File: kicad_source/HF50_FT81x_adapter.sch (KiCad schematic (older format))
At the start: 2 parts

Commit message: made layout
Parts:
- P1: renamed from P?; footprint mechanical-connectors:DSUB-9_Female_Horizontal_P2.77x2.84mm_EdgePinOffset7.70mm_Housed_MountingHolesOffset9.12mm -> Connector_Dsub:DSUB-9_Male_Horizontal_P2.77x2.84mm_EdgePinOffset7.70mm_Housed_MountingHolesOffset9.12mm
- P2: renamed from P?; footprint (none) -> mechanical-connectors:MiniDIN_8
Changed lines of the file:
@@
 $EndDescr
 $Comp
-L mechanical-connectors:CONN_01X09 P?
+L mechanical-connectors:CONN_01X09 P1
 U 1 1 609D1868
 P 3400 3250
-F 0 "P?" H 3317 3865 50  0000 C CNN
+F 0 "P1" H 3317 3865 50  0000 C CNN
 F 1 "CONN_01X09" H 3317 3774 50  0000 C CNN
-F 2 "mechanical-connectors:DSUB-9_Female_Horizontal_P2.77x2.84mm_EdgePinOffset7.70mm_Housed_MountingHolesOffset9.12mm" H 3400 3250 50  0001 C CNN
+F 2 "Connector_Dsub:DSUB-9_Male_Horizontal_P2.77x2.84mm_EdgePinOffset7.70mm_Housed_MountingHolesOffset9.12mm" H 3400 3250 50  0001 C CNN
 F 3 "" H 3400 3250 50  0000 C CNN
 	1    3400 3250
@@
 $EndComp
 $Comp
-L mechanical-connectors:CONN_01X08 P?
+L mechanical-connectors:CONN_01X08 P2
 U 1 1 609D1DBC
 P 7450 3400
-F 0 "P?" H 7528 3441 50  0000 L CNN
+F 0 "P2" H 7528 3441 50  0000 L CNN
 F 1 "CONN_01X08" H 7528 3350 50  0000 L CNN
-F 2 "" H 7450 3400 50  0000 C CNN
+F 2 "mechanical-connectors:MiniDIN_8" H 7450 3400 50  0001 C CNN
 F 3 "" H 7450 3400 50  0000 C CNN
 	1    7450 3400
@@
 PTT
 $Comp
-L power-supply:GND #PWR?
+L power-supply:GND #PWR01
 U 1 1 609D3626
 P 3800 3750
-F 0 "#PWR?" H 3800 3500 50  0001 C CNN
+F 0 "#PWR01" H 3800 3500 50  0001 C CNN
 F 1 "GND" H 3805 3577 50  0000 C CNN
 F 2 "" H 3800 3750 50  0000 C CNN
@@
 NoConn ~ 3600 3650
 $Comp
-L power-supply:GND #PWR?
+L power-supply:GND #PWR02
 U 1 1 609D3D93
 P 7100 3850
-F 0 "#PWR?" H 7100 3600 50  0001 C CNN
+F 0 "#PWR02" H 7100 3600 50  0001 C CNN
 F 1 "GND" H 7105 3677 50  0000 C CNN
 F 2 "" H 7100 3850 50  0000 C CNN

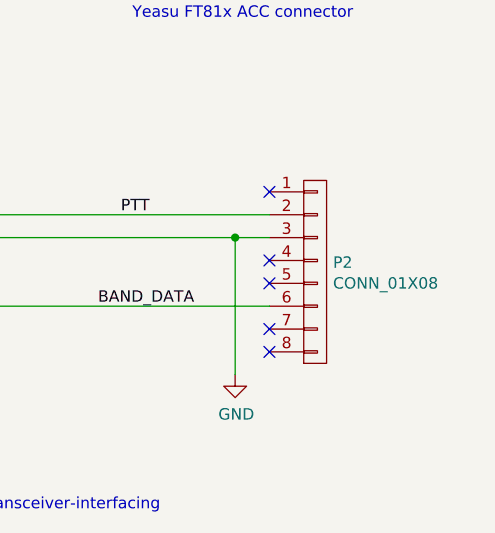
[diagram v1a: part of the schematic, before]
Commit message: added pdf schematic
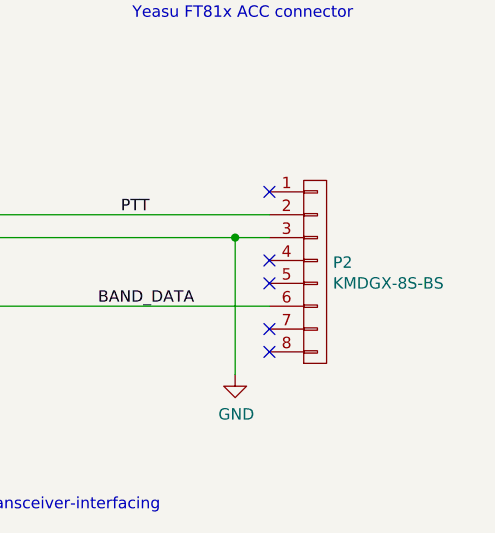
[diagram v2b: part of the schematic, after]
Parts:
- P2: value CONN_01X08 -> KMDGX-8S-BS
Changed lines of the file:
@@
 P 7450 3400
 F 0 "P2" H 7528 3441 50  0000 L CNN
-F 1 "CONN_01X08" H 7528 3350 50  0000 L CNN
+F 1 "KMDGX-8S-BS" H 7528 3350 50  0000 L CNN
 F 2 "mechanical-connectors:MiniDIN_8" H 7450 3400 50  0001 C CNN
 F 3 "" H 7450 3400 50  0000 C CNN

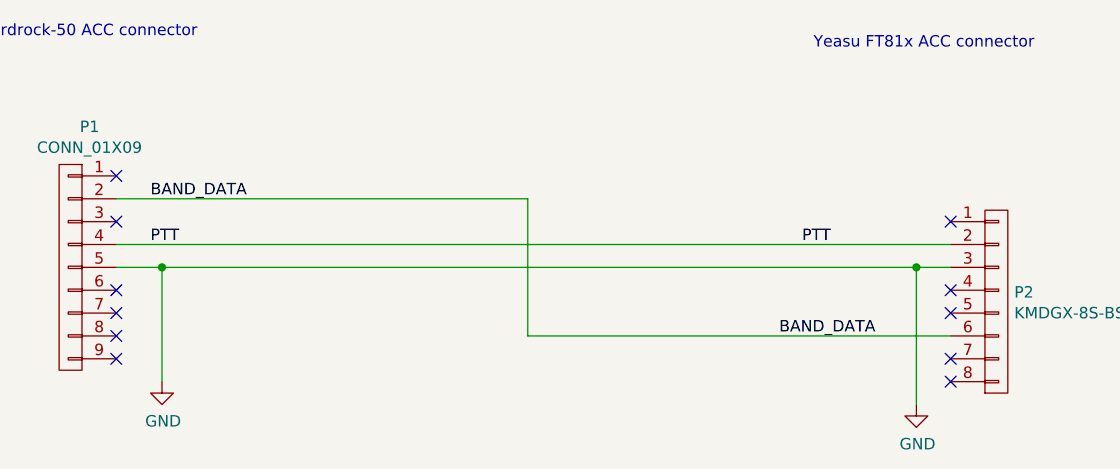
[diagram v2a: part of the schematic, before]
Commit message: added LED
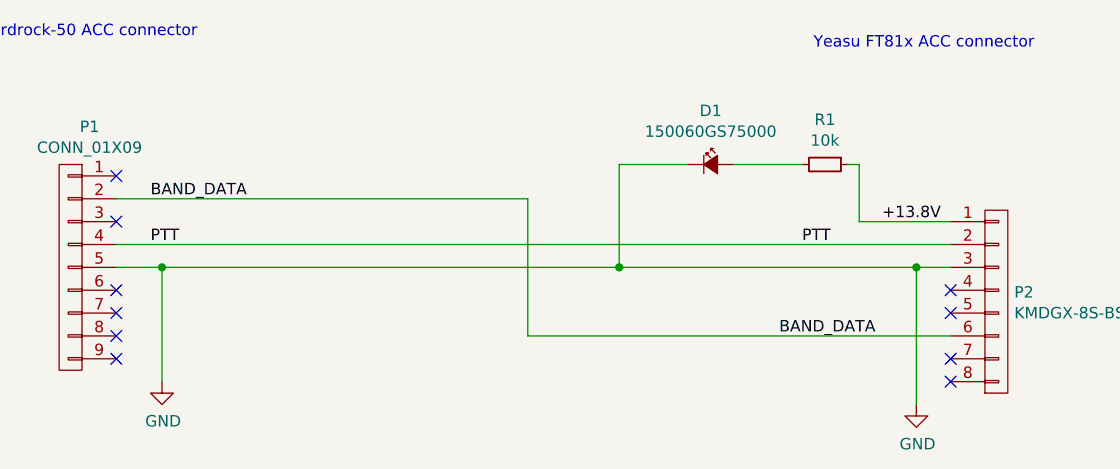
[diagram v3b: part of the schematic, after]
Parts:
- added D1: 150060GS75000, LEDs:LED_0603, symbol devices:Led_Small
- added R1: 10k, resistors:R_0603, symbol devices:R_0603
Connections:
- net GND: now also D1.1 (K)
- net +13.8V: now reaches P2.1 (P1)
- net +13.8V: now also R1.1
- new net: D1.2 (A), R1.2
- no-connect marks 11 -> 10
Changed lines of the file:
@@
 Sheet 1 1
 Title "Hardrock HF50 to Yaesu FT81x adapter"
-Date "2021-05-13"
+Date "2021-05-20"
 Rev "0.1"
 Comp "generationmake"
@@
 	3600 3150 7250 3150
 Wire Wire Line
-	7100 3250 3800 3250
+	7100 3250 5800 3250
 Connection ~ 7100 3250
 Connection ~ 3800 3250
@@
 Wire Wire Line
 	3600 2950 5400 2950
-NoConn ~ 7250 3050
 NoConn ~ 7250 3350
 NoConn ~ 7250 3450
@@
 Wire Wire Line
 	5400 3550 7250 3550
+$Comp
+L devices:R_0603 R1
+U 1 1 60A60105
+P 6700 2800
+F 0 "R1" V 6504 2800 50  0000 C CNN
+F 1 "10k" V 6595 2800 50  0000 C CNN
+F 2 "resistors:R_0603" H 6700 2650 50  0001 C CNN
+F 3 "" H 6700 2800 50  0000 C CNN
+	1    6700 2800
+	0    1    1    0
+$EndComp
+$Comp
+L devices:Led_Small D1
+U 1 1 60A6083A
+P 6200 2800
+F 0 "D1" H 6200 3035 50  0000 C CNN
+F 1 "150060GS75000" H 6200 2944 50  0000 C CNN
+F 2 "LEDs:LED_0603" V 6200 2800 50  0001 C CNN
+F 3 "" V 6200 2800 50  0000 C CNN
+	1    6200 2800
+	1    0    0    -1
+$EndComp
+Wire Wire Line
+	7250 3050 6850 3050
+Wire Wire Line
+	6850 3050 6850 2800
+Wire Wire Line
+	6850 2800 6800 2800
+Wire Wire Line
+	6600 2800 6300 2800
+Wire Wire Line
+	6100 2800 5800 2800
+Wire Wire Line
+	5800 2800 5800 3250
+Connection ~ 5800 3250
+Wire Wire Line
+	5800 3250 3800 3250
+Text Label 6950 3050 0    50   ~ 0
++13.8V
 $EndSCHEMATC

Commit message: added mounting holes
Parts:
- added MECH1, MECH2: MHP_3.2_5.0, MECH_mounting_holes:MHP_3.2_5.0, symbol MECH_mounting-holes:MHP_3.2_5.0
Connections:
- no-connect marks 10 -> 12
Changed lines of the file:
@@
 Text Label 6950 3050 0    50   ~ 0
 +13.8V
+$Comp
+L MECH_mounting-holes:MHP_3.2_5.0 MECH1
+U 1 1 60A6CF72
+P 10400 6050
+F 0 "MECH1" H 10528 6096 50  0000 L CNN
+F 1 "MHP_3.2_5.0" H 10528 6005 50  0000 L CNN
+F 2 "MECH_mounting_holes:MHP_3.2_5.0" H 10300 6100 50  0001 C CNN
+F 3 "" H 10400 6050 50  0001 C CNN
+	1    10400 6050
+	1    0    0    -1
+$EndComp
+$Comp
+L MECH_mounting-holes:MHP_3.2_5.0 MECH2
+U 1 1 60A6D7B3
+P 10400 6300
+F 0 "MECH2" H 10528 6346 50  0000 L CNN
+F 1 "MHP_3.2_5.0" H 10528 6255 50  0000 L CNN
+F 2 "MECH_mounting_holes:MHP_3.2_5.0" H 10300 6350 50  0001 C CNN
+F 3 "" H 10400 6300 50  0001 C CNN
+	1    10400 6300
+	1    0    0    -1
+$EndComp
+NoConn ~ 10100 6050
+NoConn ~ 10100 6300
 $EndSCHEMATC

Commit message: updated BOM and images, added link to aisler
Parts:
- P1: value CONN_01X09 -> LD09P33E4GX00LF
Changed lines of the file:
@@
 P 3400 3250
 F 0 "P1" H 3317 3865 50  0000 C CNN
-F 1 "CONN_01X09" H 3317 3774 50  0000 C CNN
+F 1 "LD09P33E4GX00LF" H 3317 3774 50  0000 C CNN
 F 2 "Connector_Dsub:DSUB-9_Male_Horizontal_P2.77x2.84mm_EdgePinOffset7.70mm_Housed_MountingHolesOffset9.12mm" H 3400 3250 50  0001 C CNN
 F 3 "" H 3400 3250 50  0000 C CNN
